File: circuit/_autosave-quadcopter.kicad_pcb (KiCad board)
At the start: 4 copper layers, 37.7 x 37.7 mm, 116 parts, among them J1 Conn_01x01_Female, J10 Conn_01x01_Female, J11 Conn_01x04_Male, J12 Conn_01x04_Male, J13 Conn_01x01_Female, J15 Conn_01x01_Female, J16 Conn_01x01_Female, J17 Conn_01x01_Female, J18 USB_C_Receptacle_USB2.0, J19 Conn_01x08_Male, J2 Conn_01x01_Female, J21 Conn_01x01_Female, J22 Conn_01x01_Female, J23 Conn_01x01_Female, J24 Conn_01x01_Female, J25 Conn_01x01_Female, J26 Conn_01x01_Female, J28 Conn_01x01_Female, J29 Conn_01x01_Female, J3 Conn_01x01_Female, J30 Conn_01x01_Female, J31 Conn_01x01_Female, J32 Conn_01x01_Female, J33 Conn_01x01_Female, J34 Conn_01x01_Female, J37 Conn_01x01_Female, J4 Conn_01x01_Female, J40 Conn_01x01_Female, J41 Conn_01x01_Female, J42 Conn_01x01_Female, J43 Conn_01x01_Female, J44 Conn_01x01_Female, J45 Conn_01x01_Female, J46 Conn_01x01_Female, J47 Conn_01x01_Female, J48 Conn_01x01_Female, J49 Conn_01x01_Female, J5 Conn_Coaxial, J50 Conn_01x01_Female, J6 Conn_01x06_Male, J7 Conn_01x01_Female, J8 Conn_01x01_Female, J9 Conn_01x01_Female, SW1 SW_DIP_x01, U1 STM32G474CEU6, U2 ICM-42605, U3 DPS310, U4 3V3, U5 EUP3458 1.2A, 30V max input, 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, U6 2450FM07D0034T, U7 W25Q80DVUXIE TR (16M), U8 SX1281, U9 5v, 500mA, Y1 16M, Y2 52Mhz, 12pF

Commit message: replaced pads with header for ST-link connection.
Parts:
- removed J1, J2, J34: Conn_01x01_Female, TestPoint:TestPoint_Pad_1.0x1.0mm
- moved J12 6.21 mm to (150.8, 78.3), turned to 135 degrees
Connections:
- J12 pad 2: /NRST -> /SWDIO
- J12 pad 3: /SWDIO -> /SWCLK
- J12 pad 4: /SWCLK -> /NRST
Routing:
- net /SCL2: track 26.1 -> 19.7 mm
- net /SWDIO: track 20.3 -> 14.4 mm, vias 2 -> 0
- net /NRST: track 18.1 -> 13.7 mm, vias 3 -> 2
- net GND: track 76.2 -> 79.0 mm
- net /SWCLK: track 10.3 -> 12.1 mm, vias 1 -> 0
- net +3V3: track 63.8 -> 62.3 mm

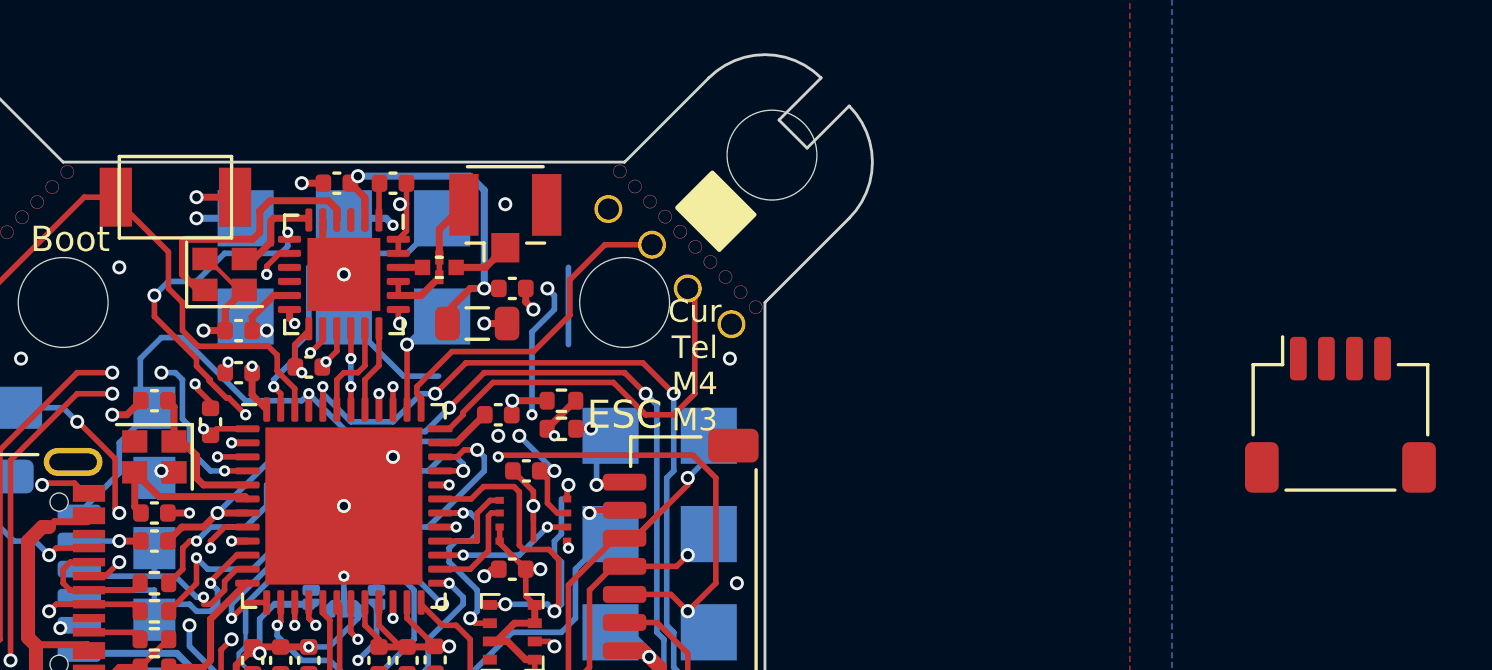
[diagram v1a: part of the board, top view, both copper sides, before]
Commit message: Cleanup work on ELRS, esp re sx1280
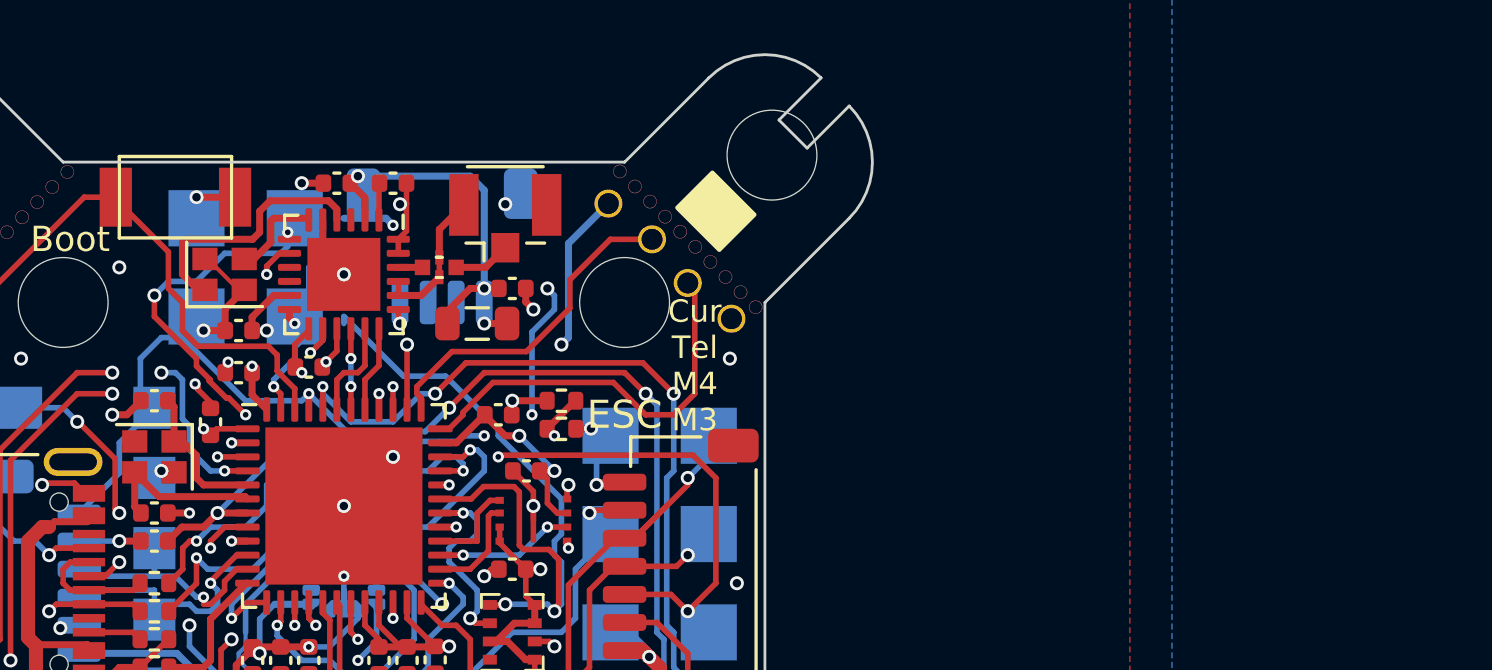
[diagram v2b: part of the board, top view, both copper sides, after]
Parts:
- removed J15, J46: Conn_01x01_Female, TestPoint:TestPoint_Pad_2.0x2.0mm
- J11: moved to B.Cu
- moved J11 32.6 mm to (140.5, 75.5)
- moved J30 3.91 mm to (131.8, 74.5)
- moved J48 3.91 mm to (131.8, 78.0)
- moved J49 1.75 mm to (135.2, 78.0)
- moved J50 1.75 mm to (135.2, 74.5)
- moved J12 0.19 mm to (150.8, 78.1)
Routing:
- net /NRST: track 13.7 -> 24.8 mm, vias 2 -> 3
- net /SCL2: track 19.7 -> 26.1 mm
- net /SDA1: track 11.2 -> 6.39 mm
- net /SCL1: track 3.98 -> 2.31 mm
- net +3V3: track 62.3 -> 63.8 mm
- net GND: track 79.0 -> 80.3 mm, vias 47 -> 46
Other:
- board text added: "I2C"
- board text removed: "C"
- board text removed: "D"
- board text removed: "I2C (GPS etc)"
- board text removed: "R"

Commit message: More work on sx1280 driver/elrs
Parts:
- Y2: footprint Crystal:Crystal_SMD_2016-4Pin_2.0x1.6mm -> Crystal:Crystal_SMD_3225-4Pin_3.2x2.5mm
- moved Y2 1.46 mm to (131.5, 77.2), turned to -90 degrees
- moved C29 0.71 mm to (133.8, 78.0), turned to 90 degrees
- moved J48 0.50 mm to (131.8, 77.5)
- moved J49 0.50 mm to (135.2, 77.5)
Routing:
- net /V_DCC: track 21.6 -> 61.4 mm, vias 3 -> 9
- net /SDA2: track 24.9 -> 0.00 mm, vias 5 -> 1
- net /V_DCC2: track 9.15 -> 0.00 mm, vias 2 -> 0
- net /BOOT0: track 19.9 -> 10.8 mm
- net /SDA1: track 6.39 -> 0.00 mm, vias 1 -> 0
- net GND: track 80.3 -> 76.2 mm
- net /SCL2: track 26.1 -> 22.8 mm
- net Net-(U8-Pad6): track 3.37 -> 6.14 mm
- net /ELRS_BUSY: track 15.6 -> 13.0 mm
- net Net-(U8-Pad4): track 9.24 -> 7.51 mm
- net +3V3: track 63.8 -> 62.6 mm, vias 15 -> 14
- net /UART1_RX: track 55.0 -> 54.4 mm

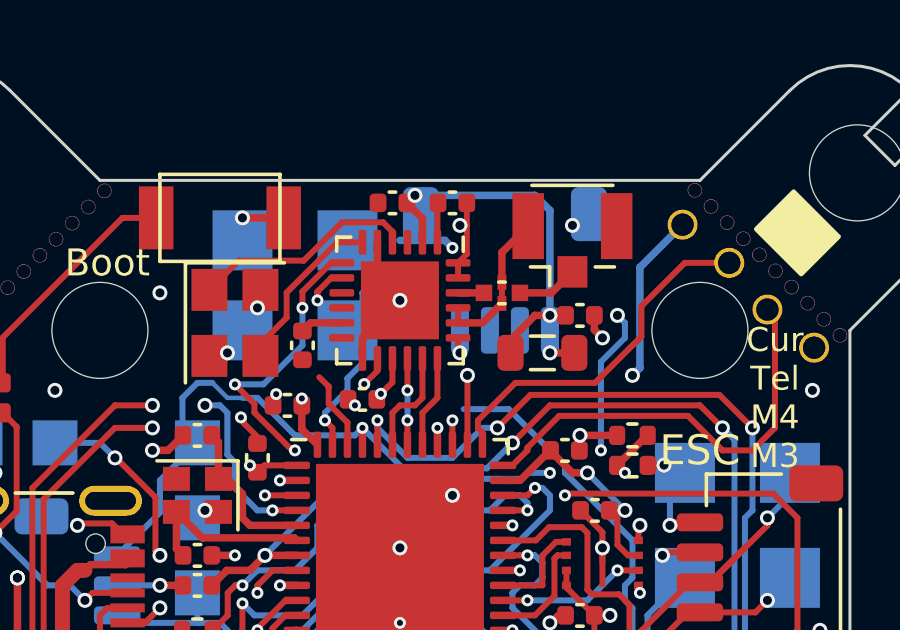
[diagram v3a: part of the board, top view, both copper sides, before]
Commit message: More work on ELRS
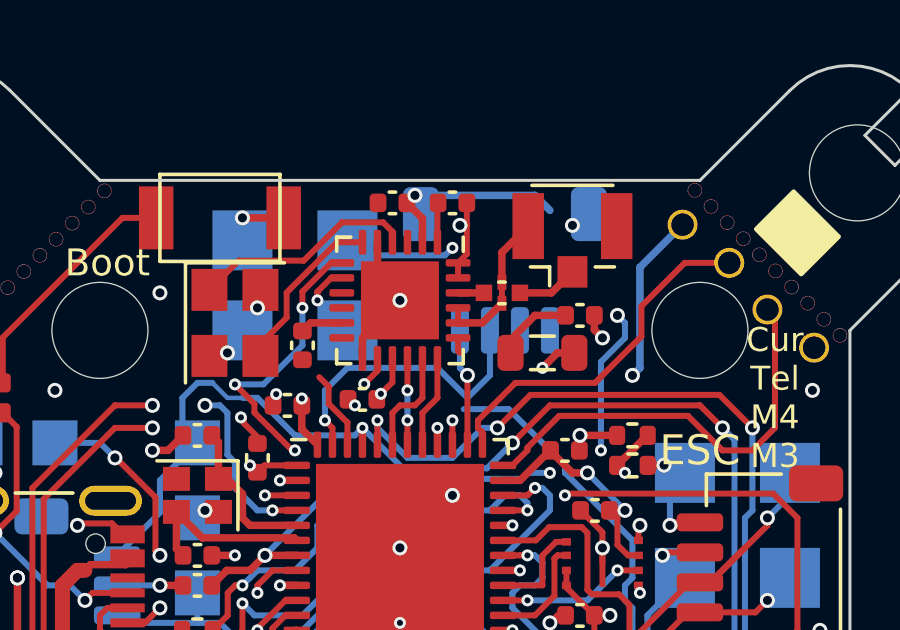
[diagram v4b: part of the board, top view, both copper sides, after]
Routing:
- net /V_DCC: track 61.4 -> 17.5 mm, vias 9 -> 1
- net /SDA2: track 0.00 -> 26.9 mm, vias 1 -> 5
- net /SDA1: track 0.00 -> 9.95 mm, vias 0 -> 1
- net /V_DCC2: track 0.00 -> 9.15 mm, vias 0 -> 2
- net /SCL1: track 2.31 -> 3.92 mm
- net /CS_ELRS: vias 3 -> 2
